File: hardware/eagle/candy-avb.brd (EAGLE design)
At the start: 58 x 85.5 mm, 162 parts, among them IC1 TPS2115ASON, IC11 ADAU1761ORIGINAL, IC2 TPS63061, IC3 10M08SCUBGA169, IC4 CP2012N-20, IC5 ADAU1761ORIGINAL, IC6 DP83848, IC7 MIC5219-3.3YM5, IC9 TXB0108ZXYR, J2 TE_MODULAR_JACK_1734577-1TOP, J4 2X6 FEMALE, X1 48MHz, X2 USBi, X3 USB Blaster

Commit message: Release v0.3.
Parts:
- added TP10, TP11, TP12, TP13, TP14, TP15, TP16, TP17, TP18, TP19, TP2, TP20, TP21, TP3, TP4, TP5, TP6, TP7, TP8, TP9, UART_CTS, UART_RTS, UART_RX, UART_TX: TPB1,27, testpad:B1,27
- moved C16 1.53 mm to (2.86, 55.7)
- moved R44 1.52 mm to (2.87, 56.8)
- moved R37 1.03 mm to (18.1, 54.0)
- moved R39 1.03 mm to (18.1, 56.1)
- moved R48 1.03 mm to (18.1, 57.2)
- moved R49 1.03 mm to (18.1, 58.3)
- moved R53 1.03 mm to (18.1, 52.9)
- moved R38 1.03 mm to (18.1, 55.0)
- moved R40 1.03 mm to (18.1, 59.4)
- moved JP1 0.48 mm to (17.4, 28.8)
- moved R25 0.30 mm to (16.4, 29.0)
- moved R26 0.30 mm to (19.6, 29.0)
- moved R27 0.30 mm to (20.7, 29.0)
- moved R28 0.30 mm to (18.5, 29.0)
- moved R29 0.30 mm to (17.4, 29.0)
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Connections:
- new net CLK2MAC: IC6.25, TP21.TP
- new net E3: IC3.E3, J4.14
- new net E4: IC3.E4, J4.4
- new net LED_SPD: IC6.27, TP20.TP
- new net RX_DV: IC6.39, TP19.TP
- net COL: now also TP5.TP
- net CRS: now also TP3.TP
- net EINT: now also TP16.TP
- net L2: no longer J4.4
- net LS_A2: now also IC3.A2; no longer IC3.B3
- net LS_A3: now also IC3.B3; no longer IC3.A2
- net MDC: now also TP18.TP
- net MDIO: now also TP17.TP
- net N3: no longer J4.14
- net RXD0: now also TP6.TP
- net RXD1: now also TP7.TP
- net RXD2: now also TP8.TP
- net RXD3: now also TP9.TP
- net RX_CLK: now also TP2.TP
- net RX_ER: now also TP4.TP
- net TXD0: now also TP12.TP
- net TXD1: now also TP13.TP
- net TXD2: now also TP14.TP
- net TXD3: now also TP15.TP
- net TXEN: now also TP11.TP
- net TX_CLK: now also TP10.TP
- net UART_CTS: now also UART_CTS.TP
- net UART_RTS: now also UART_RTS.TP
- net UART_RX: now also UART_RX.TP
- net UART_TX: now also UART_TX.TP
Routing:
- net E3: track 0.00 -> 39.9 mm, vias 0 -> 2
- net N3: track 35.7 -> 0.00 mm
- net E4: track 0.00 -> 23.0 mm, vias 0 -> 2
- net L2: track 21.8 -> 0.00 mm
- net RX_DV: track 0.00 -> 10.3 mm, vias 0 -> 2
- net CLK2MAC: track 0.00 -> 6.17 mm, vias 0 -> 2
- net LED_SPD: track 0.00 -> 5.99 mm, vias 0 -> 2
- net TXD0: track 12.7 -> 16.4 mm
- net TXD2: track 15.0 -> 18.6 mm
- net TXD1: track 14.8 -> 18.1 mm
- net TXD3: track 19.2 -> 22.4 mm
- net TXEN: track 12.5 -> 15.3 mm
- net TX_CLK: track 9.61 -> 12.2 mm
- net EINT: track 22.0 -> 24.4 mm
- net MDIO: track 23.3 -> 25.5 mm
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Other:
- board text added: "ADC Pins"
- board text added: "Add Test Pad CP2102N UART line."
- board text added: "Add Test Pad DP83848 Ethernet line."
- board text added: "B1:E3"
- board text added: "C1 L3"
- board text added: "C2 N2"
- board text added: "D1 M2"
- board text added: "E1 M1"
- board text added: "F1:E4"
- board text added: "GND:3V3"
- board text added: "H1:D2"
- board text added: "v0.3"
- board text added: "v0.3: Fix C3 GND Pin connection."
- board text removed: "B1/N3"
- board text removed: "C1/L3"
- board text removed: "C2/N2"
- board text removed: "D1/M2"
- board text removed: "E1/M1"
- board text removed: "F1/D2"
- board text removed: "F1/L2"
- board text removed: "GND/3V3"
- board text removed: "v0.2"

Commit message: Release v0.4.
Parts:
- moved X3 1.27 mm to (30.2, 26.5), turned to 90 degrees
- renumbered USER_SW to RESET_SW
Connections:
- net BITCLOCK: now also IC3.M5; no longer IC3.N5
- net COL: now also IC3.N11; no longer IC3.L10
- net CRS: now also IC3.N12; no longer IC3.M11
- net DATA_IN: now also IC3.N5; no longer IC3.M5
- net DATA_OUT: now also IC3.K6; no longer IC3.N6
- net DATA_OUT_2: now also IC3.L5; no longer IC3.N4
- net LRCLOCK: now also IC3.N4; no longer IC3.L5
- net RXD0: now also IC3.L10; no longer IC3.N11
- net RXD1: now also IC3.N10; no longer IC3.M10
- net RXD2: now also IC3.M10; no longer IC3.N10
- net RXD3: now also IC3.N9; no longer IC3.M9
- net RX_CLK: now also IC3.L11; no longer IC3.M12
- net RX_DV: now also IC3.M12
- net RX_ER: now also IC3.M11; no longer IC3.N12
- net TXD0: now also IC3.M8; no longer IC3.N8
- net TXD1: now also IC3.N7; no longer IC3.M7
- net TXD2: now also IC3.M7; no longer IC3.N7
- net TXD3: now also IC3.N6; no longer IC3.K6
- net TXEN: now also IC3.N8; no longer IC3.M8
- net TX_CLK: now also IC3.M9; no longer IC3.N9
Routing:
- net MCLK: track 20.5 -> 60.3 mm
- net CLK0N: track 8.70 -> 47.1 mm
- net N$59: track 6.72 -> 35.3 mm
- net TCK: track 11.5 -> 28.1 mm
- net TDO: track 20.5 -> 29.1 mm
- net RX_DV: track 10.3 -> 18.8 mm
- net TMS: track 14.8 -> 18.6 mm
- net TDI: track 21.6 -> 18.4 mm, vias 2 -> 1
- net TXD3: track 22.4 -> 19.3 mm
- net DATA_OUT: track 17.8 -> 20.2 mm
- net DATA_OUT_2: track 31.3 -> 33.4 mm
- net RX_CLK: track 8.55 -> 10.6 mm
- net RXD0: track 5.61 -> 7.54 mm
- net LRCLOCK: track 18.5 -> 16.5 mm
- net RX_ER: track 6.18 -> 8.07 mm
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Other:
- board text added: "Change M12 from RX_CLK to RX_DV."
- board text added: "Refactoring some FPGA pins connection."
- board text added: "Rotate the X1 connector 180 degrees."
- board text added: "v0.4"
- board text added: "v0.4: Connect L11 to RX_CLK."
- board text removed: "v0.3"

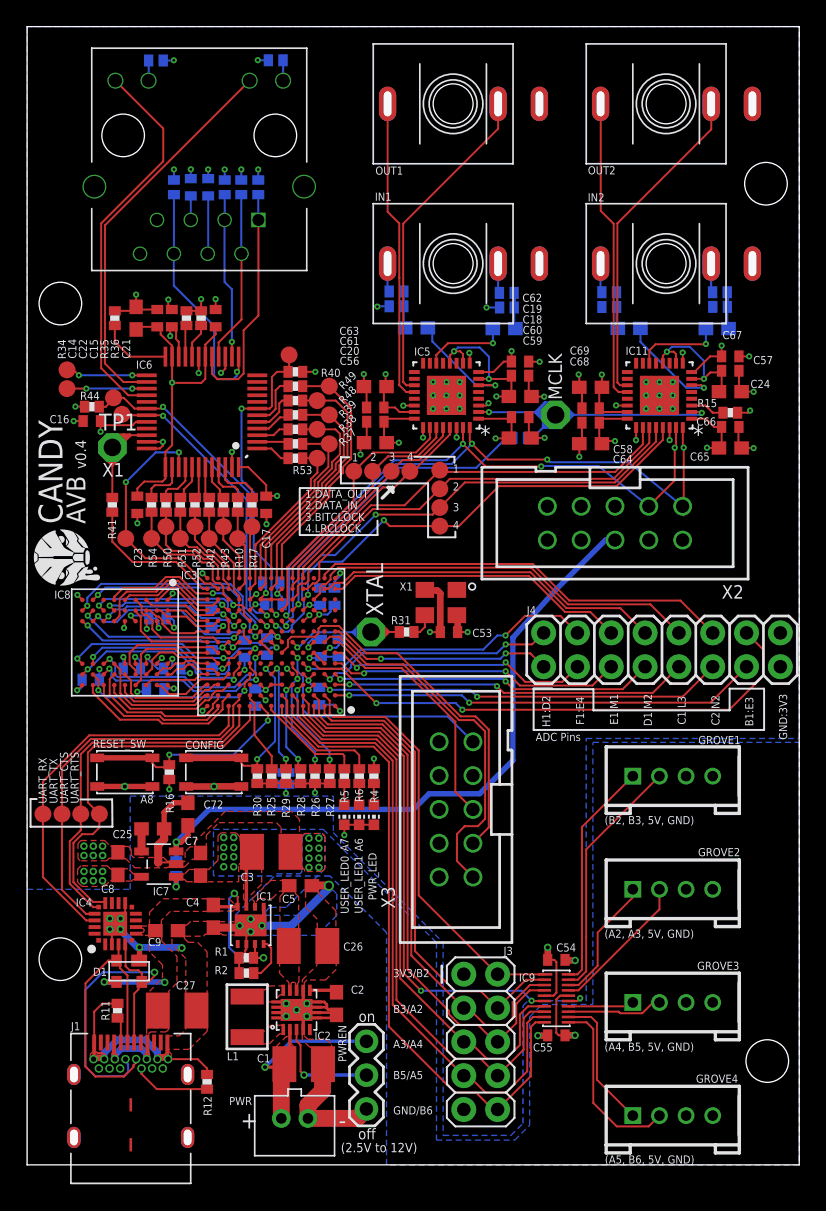
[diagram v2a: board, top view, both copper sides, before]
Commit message: Release v0.5
Change C26 from 47uF to 22uF x3.
Change C1 from 47uF to 10uF x2.
Change L1 package size.
Create GND plane on top layer.
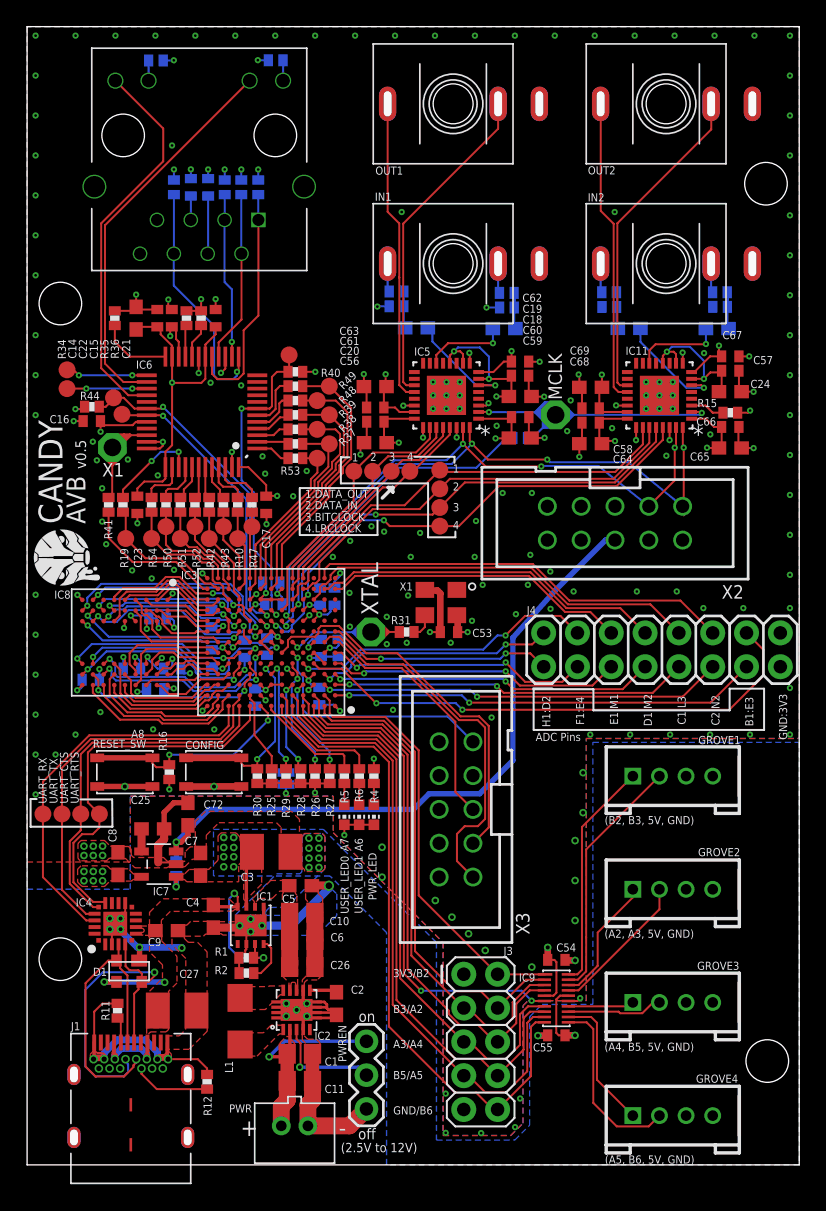
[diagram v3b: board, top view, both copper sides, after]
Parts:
- added C10, C6: 22uF, tkrworks:C0805
- added C11: 10uF, tkrworks:C0805
- added R19: 33, tkrworks:0402-RES
- C1: value 47uF -> 10uF; device tkrworks:C1210 -> tkrworks:C0805
- C14: value 10uF -> 10uF tant
- C26: value 47uF -> 22uF; device tkrworks:C1210 -> tkrworks:C0805
- L1: device tkrworks:L1210 -> tkrworks:L4240
- moved C26 1.64 mm to (18.7, 14.7)
- moved C1 0.83 mm to (18.5, 8.14)
- moved L1 0.62 mm to (14.0, 10.6)
- moved PWR 0.56 mm to (18.1, 2.73)
- moved R41 0.28 mm to (4.12, 49.4)
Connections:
- new net N$21: IC6.39, R19.2
- net BAT: now also C10.1, C6.1
- net GND: now also C10.2, C11.2, C6.2
- net RX_DV: now also R19.1; no longer IC6.39
- net VIN: now also C11.1
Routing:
- net RX_DV: track 18.8 -> 10.6 mm, vias 2 -> 0
- net N$21: track 0.00 -> 7.10 mm, vias 0 -> 2
- net GND: track 190.0 -> 195.3 mm, vias 113 -> 248
- net BAT: track 0.00 -> 4.08 mm
- net VIN: track 18.4 -> 16.9 mm
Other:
- board text added: "2.2uF"
- board text added: "Change C1 from 47uF to 10uF x2."
- board text added: "Change L1 package size."
- board text added: "Create GND plane on top layer."
- board text added: "v0.5"
- board text added: "v0.5: Change C26 from 47uF to 22uF x3."
- board text removed: "v0.4"

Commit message: Release v0.6
Add the power switch MIC2005A to reset the ADAU1772.
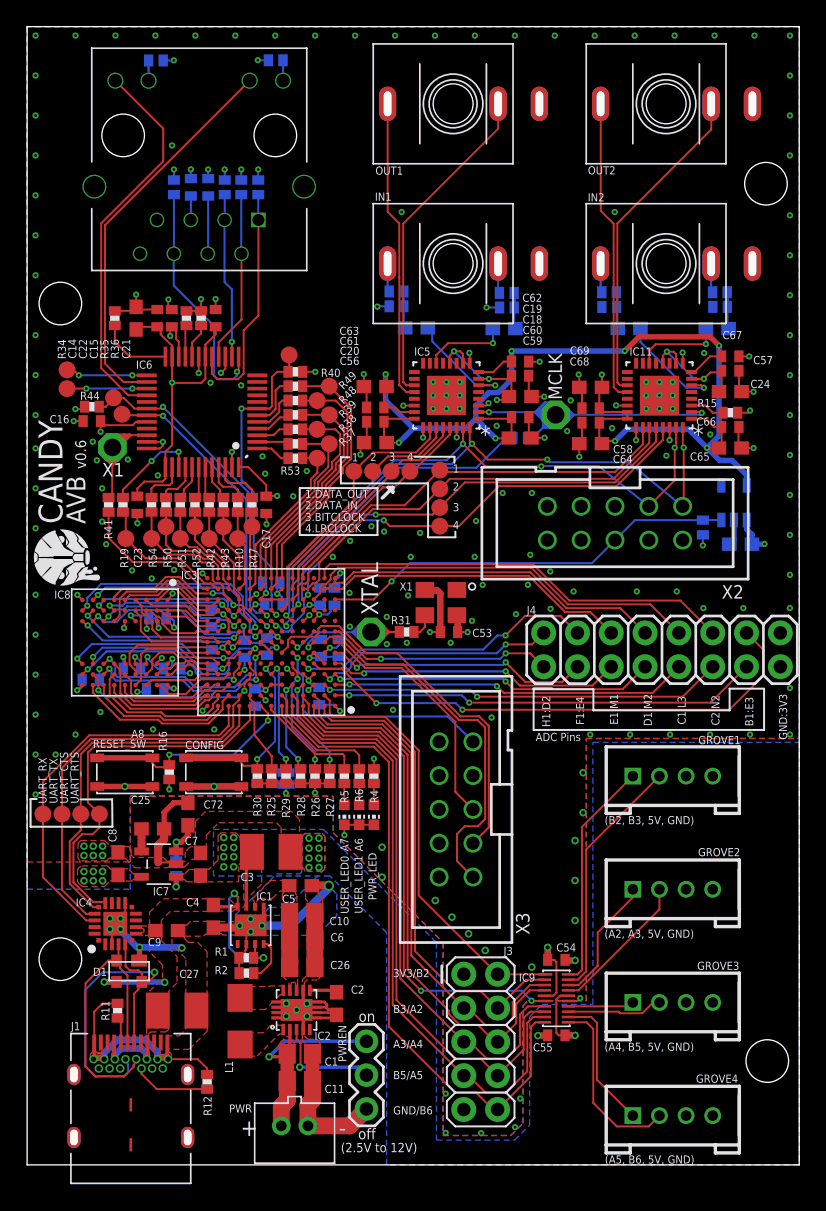
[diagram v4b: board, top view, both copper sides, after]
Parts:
- added C28: 1uF, tkrworks:C0603
- added IC10: MIC2005A, tkrworks:SOT23-5
- added R20: 10k, tkrworks:0402-RES
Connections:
- new net EN1: C72.1, IC7.3, R59.2
- new net VOUT: C20.1, C56.1, C58.1, C59.1, C60.1, C61.2, C62.2, C63.2, C64.1, C65.1, C66.1, C67.2, C68.2, C69.2, IC10.5, IC11.1, IC11.23, IC11.24, IC11.8, IC5.1, IC5.23, IC5.24, IC5.8
- net BRD_RESET: now also IC10.3, IC3.L1, R20.2; no longer C72.1, IC7.3, R59.2
- net GND: now also C28.2, IC10.2
- net VDD: now also C28.1, IC10.1, R20.1; no longer C20.1, C56.1, C58.1, C59.1, C60.1, C61.2, C62.2, C63.2, C64.1, C65.1, C66.1, C67.2, C68.2, C69.2, IC11.1, IC11.23, IC11.24, IC11.8, IC5.1, IC5.23, IC5.24, IC5.8
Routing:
- net VOUT: track 0.00 -> 94.7 mm, vias 0 -> 9
- net VDD: track 120.2 -> 86.6 mm, vias 51 -> 45
- net BRD_RESET: track 51.8 -> 31.5 mm
- net EN1: track 0.00 -> 3.94 mm, vias 0 -> 1
- net GND: track 195.3 -> 197.3 mm, vias 248 -> 251
- net SCL1: track 48.6 -> 47.3 mm
- net N$28: track 12.3 -> 11.2 mm
- net N$32: track 11.3 -> 10.2 mm
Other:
- board text added: "for the ADAU1772."
- board text added: "v0.6"
- board text added: "v0.6: Add the power swith MIC2005A"
- board text removed: "v0.5"
